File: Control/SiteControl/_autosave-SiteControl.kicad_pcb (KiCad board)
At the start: 2 copper layers, 109.2 x 48.3 mm, 114 parts, among them J1 RJ50, J2 CONN_01X02, J3 CONN_02X07, J4 CONN_01X06, J5 RS232-Jack, J6 CONN_01X02, J7 USB_A, Q1 BC817-40, Q2 Q_PJFET_GSD, U1 Opto_H11L1M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

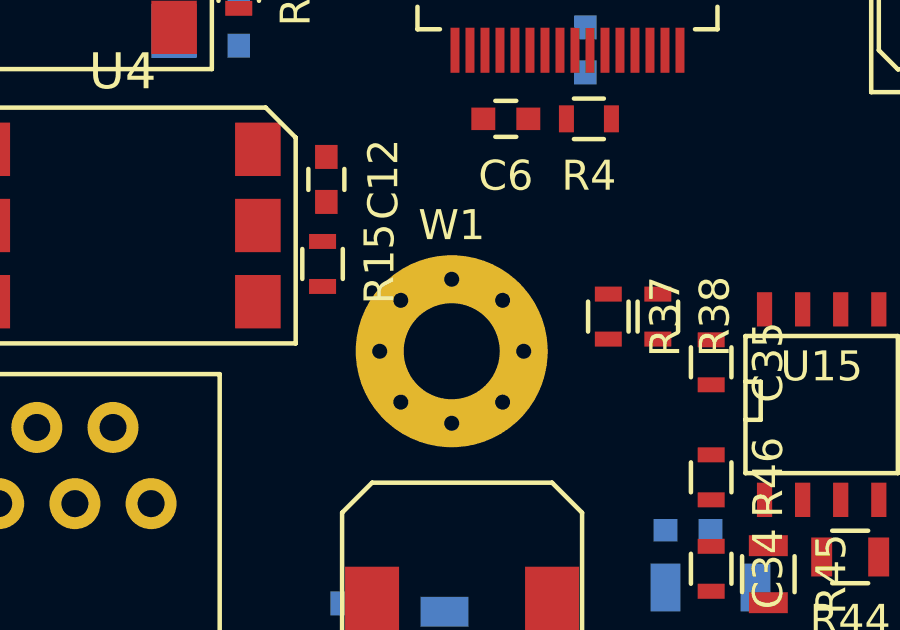
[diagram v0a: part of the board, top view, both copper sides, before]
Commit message: [Added] Mechanical drawings for control board mounting case
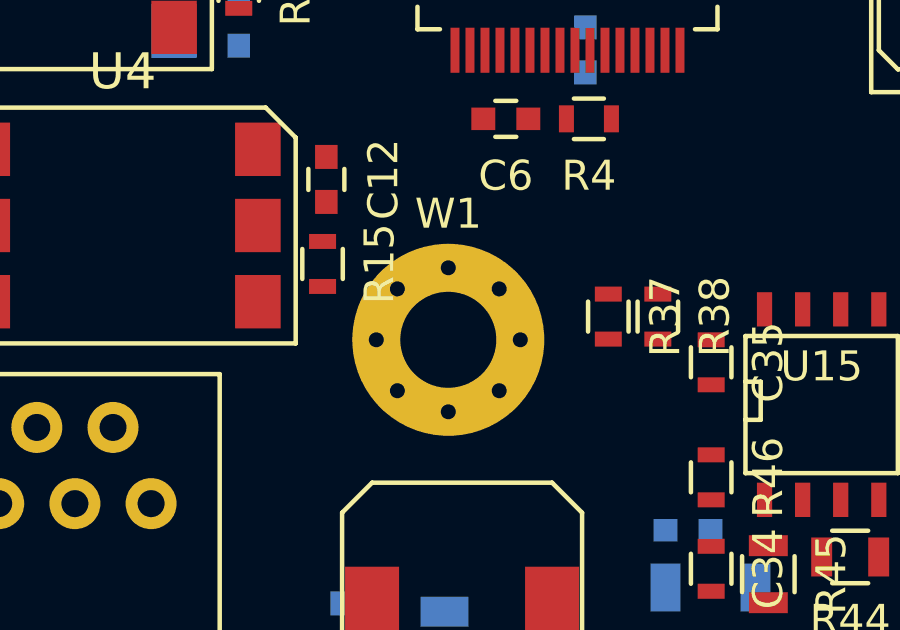
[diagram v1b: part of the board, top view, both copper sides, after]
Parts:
- moved W1 0.40 mm to (112.8, 92.3)
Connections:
- J3 pad 10: CMOS_RTS -> PiSDA
- J3 pad 11: CMOS_RX -> Net-(J3-Pad11)
- J3 pad 12: CMOS_TX -> Pi_VSense
- J3 pad 3: Pi_VSense -> CMOS_TX
- J3 pad 4: Net-(J3-Pad4) -> CMOS_RX
- J3 pad 5: PiSDA -> CMOS_RTS
- J3 pad 6: PiSDA -> CMOS_CTS
- J3 pad 9: CMOS_CTS -> PiSDA
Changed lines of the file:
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@@
   (net 115 "Net-(U12-Pad10)")
   (net 116 "Net-(U15-Pad3)")
-  (net 117 "Net-(J4-Pad6)")
-  (net 118 "Net-(J7-Pad3)")
-  (net 119 "Net-(J7-Pad2)")
-  (net 120 "Net-(J7-Pad1)")
-  (net 121 "Net-(J3-Pad4)")
+  (net 117 "Net-(J3-Pad11)")
+  (net 118 "Net-(J4-Pad6)")
+  (net 119 "Net-(J7-Pad3)")
+  (net 120 "Net-(J7-Pad2)")
+  (net 121 "Net-(J7-Pad1)")
   (net_class Default "This is the default net class."
     (clearance 0.2)
@@
     (add_net "Net-(C8-Pad1)")
     (add_net "Net-(D1-Pad1)")
-    (add_net "Net-(J3-Pad4)")
+    (add_net "Net-(J3-Pad11)")
     (add_net "Net-(J4-Pad6)")
     (add_net "Net-(J7-Pad1)")
@@
   )
   (module Mounting_Holes:MountingHole_3.2mm_M3_Pad_Via (layer F.Cu)
-    (at 112.89 92.71)
+    (at 112.776 92.329)
     (descr "Mounting Hole 3.2mm, M3")
     (tags "mounting hole 3.2mm m3")
@@
       (net 10 RPi_En))
     (pad 5 smd rect (at 0 -4.76 270) (size 1.78 1.52) (layers F.Cu F.Paste F.Mask)
-      (net 120 "Net-(J7-Pad1)"))
+      (net 121 "Net-(J7-Pad1)"))
     (pad 2 smd rect (at 0 4.76 270) (size 1.78 1.52) (layers F.Cu F.Paste F.Mask)
       (net 79 "Net-(R23-Pad2)"))
@@
       (net 2 GND))
     (pad 3 thru_hole oval (at 0 2.54 270) (size 1.7272 1.7272) (drill 1.016) (layers *.Cu *.Mask F.SilkS)
-      (net 35 Pi_VSense))
+      (net 13 CMOS_TX))
     (pad 4 thru_hole oval (at 2.54 2.54 270) (size 1.7272 1.7272) (drill 1.016) (layers *.Cu *.Mask F.SilkS)
-      (net 121 "Net-(J3-Pad4)"))
+      (net 14 CMOS_RX))
     (pad 5 thru_hole oval (at 0 5.08 270) (size 1.7272 1.7272) (drill 1.016) (layers *.Cu *.Mask F.SilkS)
-      (net 37 PiSDA))
+      (net 32 CMOS_RTS))
     (pad 6 thru_hole oval (at 2.54 5.08 270) (size 1.7272 1.7272) (drill 1.016) (layers *.Cu *.Mask F.SilkS)
-      (net 37 PiSDA))
+      (net 31 CMOS_CTS))
     (pad 7 thru_hole oval (at 0 7.62 270) (size 1.7272 1.7272) (drill 1.016) (layers *.Cu *.Mask F.SilkS)
       (net 36 PiSCL))
@@
       (net 36 PiSCL))
     (pad 9 thru_hole oval (at 0 10.16 270) (size 1.7272 1.7272) (drill 1.016) (layers *.Cu *.Mask F.SilkS)
-      (net 31 CMOS_CTS))
+      (net 37 PiSDA))
     (pad 10 thru_hole oval (at 2.54 10.16 270) (size 1.7272 1.7272) (drill 1.016) (layers *.Cu *.Mask F.SilkS)
-      (net 32 CMOS_RTS))
+      (net 37 PiSDA))
     (pad 11 thru_hole oval (at 0 12.7 270) (size 1.7272 1.7272) (drill 1.016) (layers *.Cu *.Mask F.SilkS)
-      (net 14 CMOS_RX))
+      (net 117 "Net-(J3-Pad11)"))
     (pad 12 thru_hole oval (at 2.54 12.7 270) (size 1.7272 1.7272) (drill 1.016) (layers *.Cu *.Mask F.SilkS)
-      (net 13 CMOS_TX))
+      (net 35 Pi_VSense))
     (pad 13 thru_hole oval (at 0 15.24 270) (size 1.7272 1.7272) (drill 1.016) (layers *.Cu *.Mask F.SilkS)
       (net 2 GND))
@@
       (net 40 PGEC))
     (pad 6 thru_hole oval (at 0 12.7 90) (size 2.032 1.7272) (drill 1.016) (layers *.Cu *.Mask F.SilkS)
-      (net 117 "Net-(J4-Pad6)"))
+      (net 118 "Net-(J4-Pad6)"))
     (model Pin_Headers.3dshapes/Pin_Header_Straight_1x06.wrl
       (at (xyz 0 -0.25 0))
@@
       (net 2 GND))
     (pad 3 thru_hole circle (at 4.57286 -0.00212 90) (size 1.50114 1.50114) (drill 1.00076) (layers *.Cu *.Mask F.SilkS)
-      (net 118 "Net-(J7-Pad3)"))
+      (net 119 "Net-(J7-Pad3)"))
     (pad 2 thru_hole circle (at 2.54086 -0.00212 90) (size 1.50114 1.50114) (drill 1.00076) (layers *.Cu *.Mask F.SilkS)
-      (net 119 "Net-(J7-Pad2)"))
+      (net 120 "Net-(J7-Pad2)"))
     (pad 1 thru_hole circle (at 0.00086 -0.00212 90) (size 1.50114 1.50114) (drill 1.00076) (layers *.Cu *.Mask F.SilkS)
-      (net 120 "Net-(J7-Pad1)"))
+      (net 121 "Net-(J7-Pad1)"))
     (pad 5 thru_hole circle (at 10.16086 2.66488 90) (size 2.99974 2.99974) (drill 2.30124) (layers *.Cu *.Mask F.SilkS)
       (net 2 GND))
